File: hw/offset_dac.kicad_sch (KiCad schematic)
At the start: 35 parts, among them Q1 SSM6N35AFE, Q3 SSM6N35AFE, U22 TSV992A, U23 MCP47CVB02-E_UN

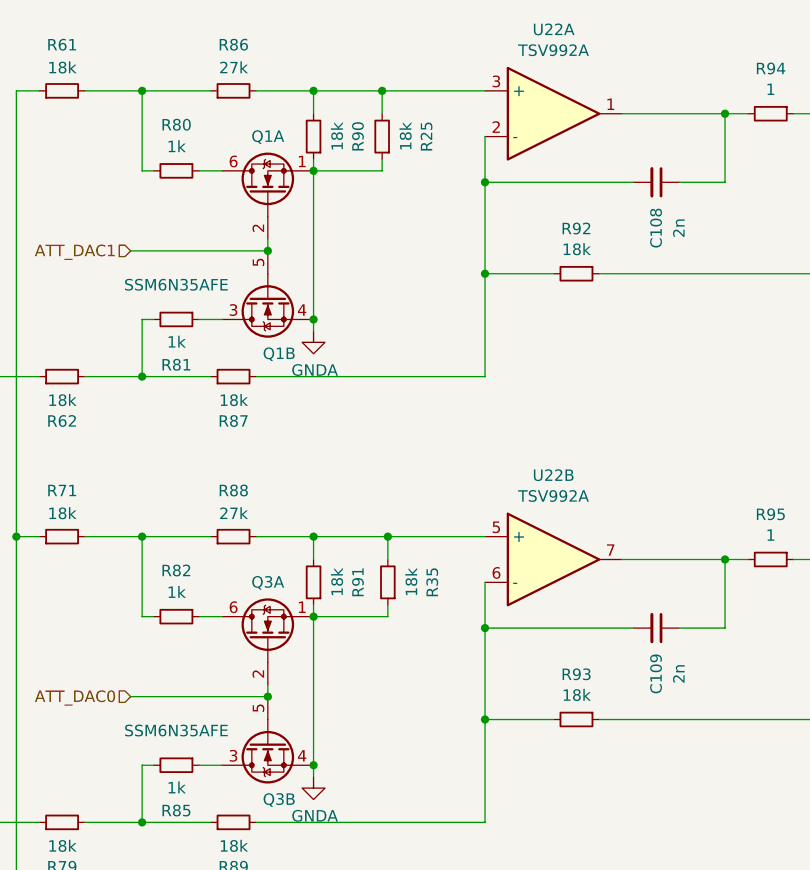
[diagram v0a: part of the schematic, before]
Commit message: Modified DAC resistors/range; connect + pull-up ADC SHDN
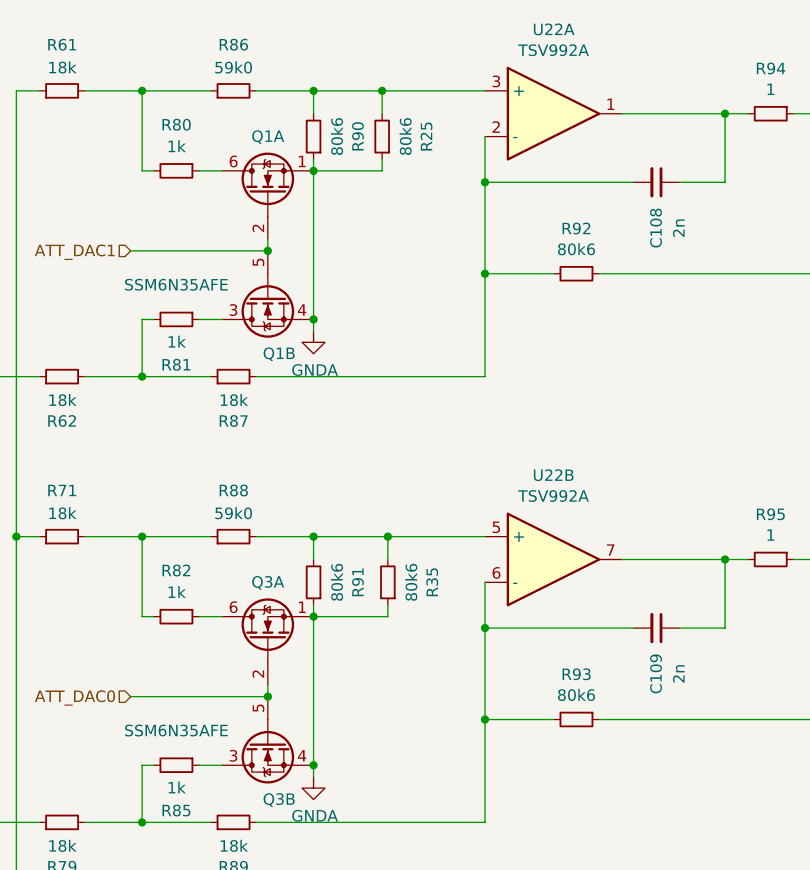
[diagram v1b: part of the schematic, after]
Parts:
- R25, R35, R90, R91, R92, R93: value 18k -> 80k6
- R86, R88: value 27k -> 59k0
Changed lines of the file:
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@@
       (effects (font (size 1.27 1.27)))
     )
-    (property "Value" "18k" (at 167.64 63.373 90)
+    (property "Value" "80k6" (at 167.64 63.373 90)
       (effects (font (size 1.27 1.27)))
     )
@@
       (effects (font (size 1.27 1.27)))
     )
-    (property "Value" "18k" (at 141.097 50.8 90)
+    (property "Value" "80k6" (at 141.097 50.8 90)
       (effects (font (size 1.27 1.27)))
     )
@@
       (effects (font (size 1.27 1.27)))
     )
-    (property "Value" "18k" (at 167.64 112.903 90)
+    (property "Value" "80k6" (at 167.64 112.903 90)
       (effects (font (size 1.27 1.27)))
     )
@@
       (effects (font (size 1.27 1.27)))
     )
-    (property "Value" "27k" (at 129.54 92.71 90)
+    (property "Value" "59k0" (at 129.54 92.71 90)
       (effects (font (size 1.27 1.27)))
     )
@@
       (effects (font (size 1.27 1.27)))
     )
-    (property "Value" "18k" (at 148.717 50.8 90)
+    (property "Value" "80k6" (at 148.717 50.8 90)
       (effects (font (size 1.27 1.27)))
     )
@@
       (effects (font (size 1.27 1.27)))
     )
-    (property "Value" "18k" (at 149.352 100.33 90)
+    (property "Value" "80k6" (at 149.352 100.33 90)
       (effects (font (size 1.27 1.27)))
     )
@@
       (effects (font (size 1.27 1.27)))
     )
-    (property "Value" "18k" (at 141.097 100.33 90)
+    (property "Value" "80k6" (at 141.097 100.33 90)
       (effects (font (size 1.27 1.27)))
     )
@@
       (effects (font (size 1.27 1.27)))
     )
-    (property "Value" "27k" (at 129.54 43.18 90)
-      (effects (font (size 1.27 1.27)))
-    )
+    (property "Value" "59k0" (at 129.54 43.18 90)
+      (effects (font (size 1.27 1.27)))
+    )

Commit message: renaming, comments, part/vendor and other cosmetics (no pcb change)
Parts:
- U22: Manufacturer (none) -> ST; Part (none) -> TSV992IQ2
- U23: Part MCP47CVB02-E_UN -> MCP47CVB02-E/UN
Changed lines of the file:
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@@
       (effects (font (size 1.27 1.27)) hide)
     )
-    (property "Part" "MCP47CVB02-E_UN" (at 105.41 152.4 0)
+    (property "Part" "MCP47CVB02-E/UN" (at 105.41 152.4 0)
       (effects (font (size 1.27 1.27)) hide)
     )
@@
       (effects (font (size 1.27 1.27)) hide)
     )
+    (property "Part" "TSV992IQ2" (at 165.1 48.26 0)
+      (effects (font (size 1.27 1.27)) hide)
+    )
+    (property "Manufacturer" "ST" (at 165.1 48.26 0)
+      (effects (font (size 1.27 1.27)) hide)
+    )
     (pin "1")
     (pin "2")
@@
     )
     (property "Sim.Pins" "1=out1 2=in1- 3=in1+ 4=vee 5=in2+ 6=in2- 7=out2 8=vcc" (at 165.1 97.79 0)
+      (effects (font (size 1.27 1.27)) hide)
+    )
+    (property "Part" "TSV992IQ2" (at 165.1 97.79 0)
+      (effects (font (size 1.27 1.27)) hide)
+    )
+    (property "Manufacturer" "ST" (at 165.1 97.79 0)
       (effects (font (size 1.27 1.27)) hide)
     )
@@
       (effects (font (size 1.27 1.27)) hide)
     )
+    (property "Part" "TSV992IQ2" (at 55.88 58.42 0)
+      (effects (font (size 1.27 1.27)) hide)
+    )
+    (property "Manufacturer" "ST" (at 55.88 58.42 0)
+      (effects (font (size 1.27 1.27)) hide)
+    )

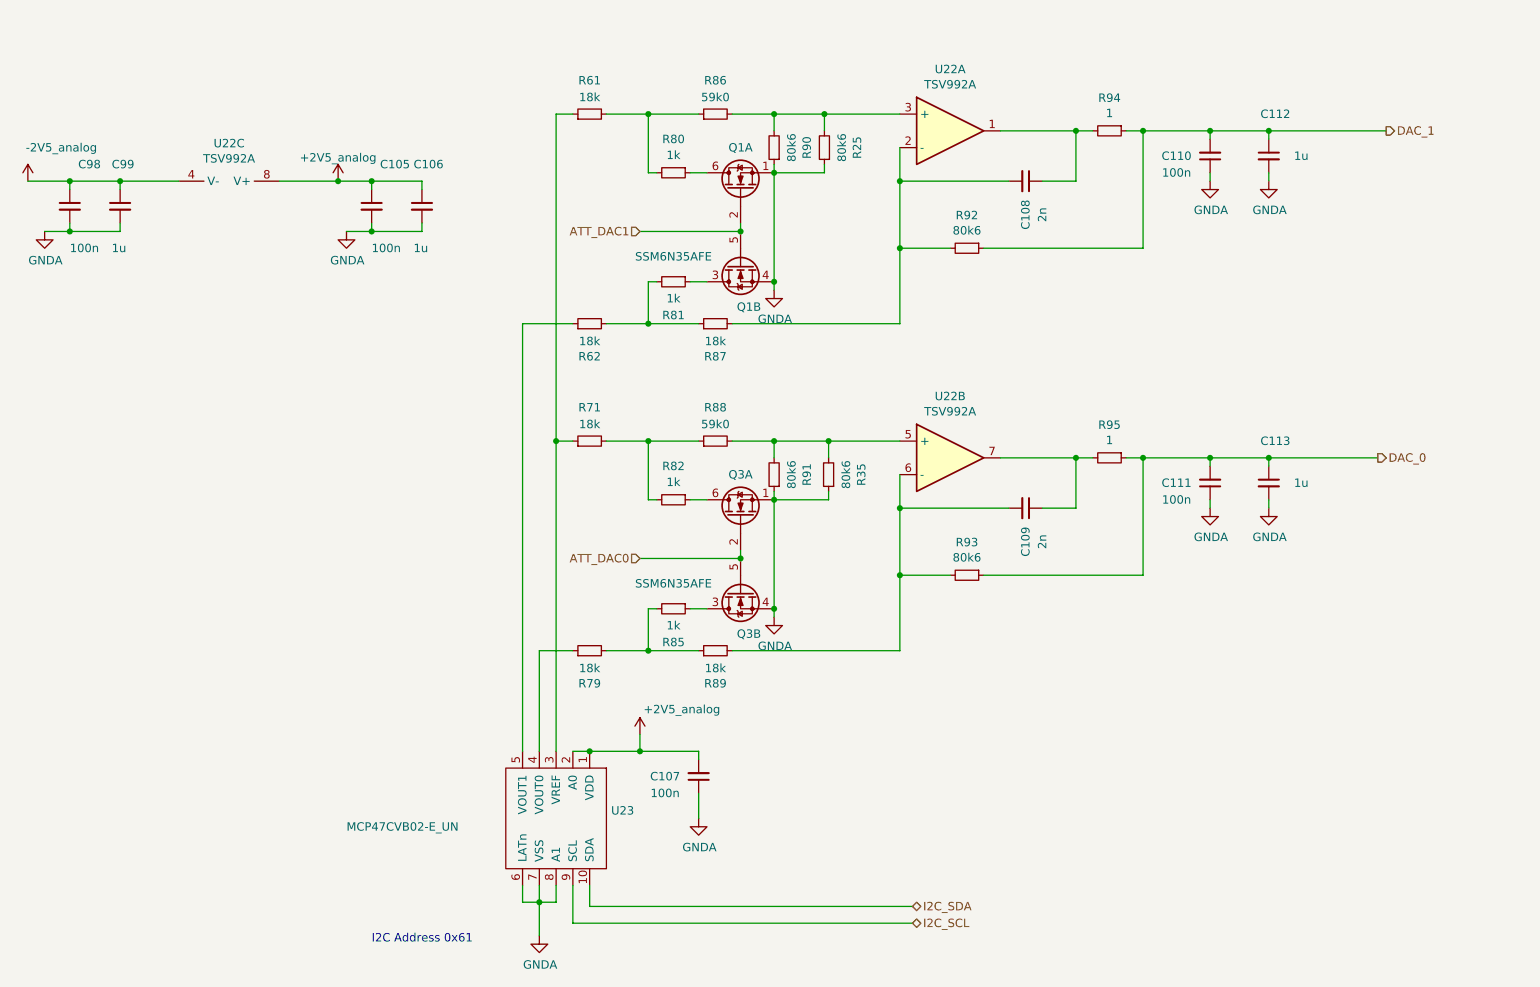
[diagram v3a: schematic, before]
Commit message: DAC noise improvements
 - increased C108, C109 from 2n to 100n
 - added C147, C148 (100n) parallel to R25, R35, respectively.
   Recycled pads of second 80k6 resistors for new capacitors
   so that the layout + stencil stay the same.

Significantly improves noise on 10kHz-100kHz band.
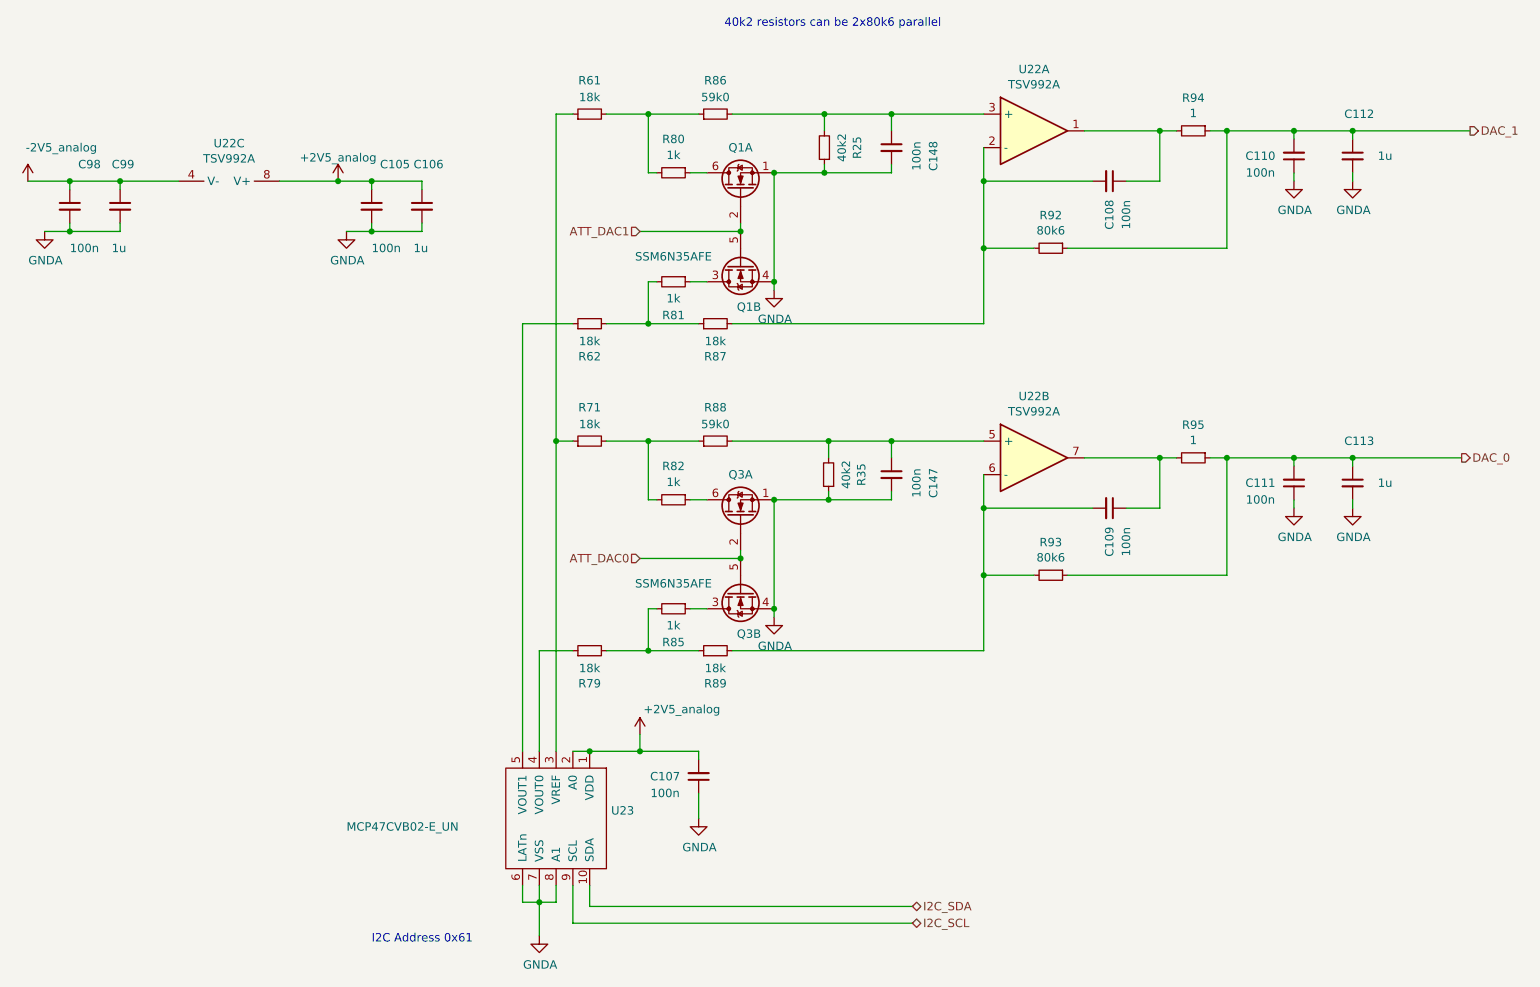
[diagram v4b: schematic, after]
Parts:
- removed R90, R91: 80k6, Resistor_SMD:R_0603_1608Metric, symbol Device:R_Small
- added C147, C148: 100n, Capacitor_SMD:C_0603_1608Metric, symbol Device:C_Small
- C108, C109: value 2n -> 100n; Manufacturer (none) -> Samsung; Part (none) -> CL10B104KB8NFN
- R25, R35: value 80k6 -> 40k2
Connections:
- net GNDA: now also C147.2, C148.2
- net at R25.2, R86.2, U22.3 (+): now also C148.1
- net at R35.2, R88.2, U22.5 (+): now also C147.1
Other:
- note added: "40k2 resistors can be 2x80k6 parallel"
- moved on the sheet: C108, C109, C110, C111, C112, C113, R92, R93, R94, R95, U22A, U22B

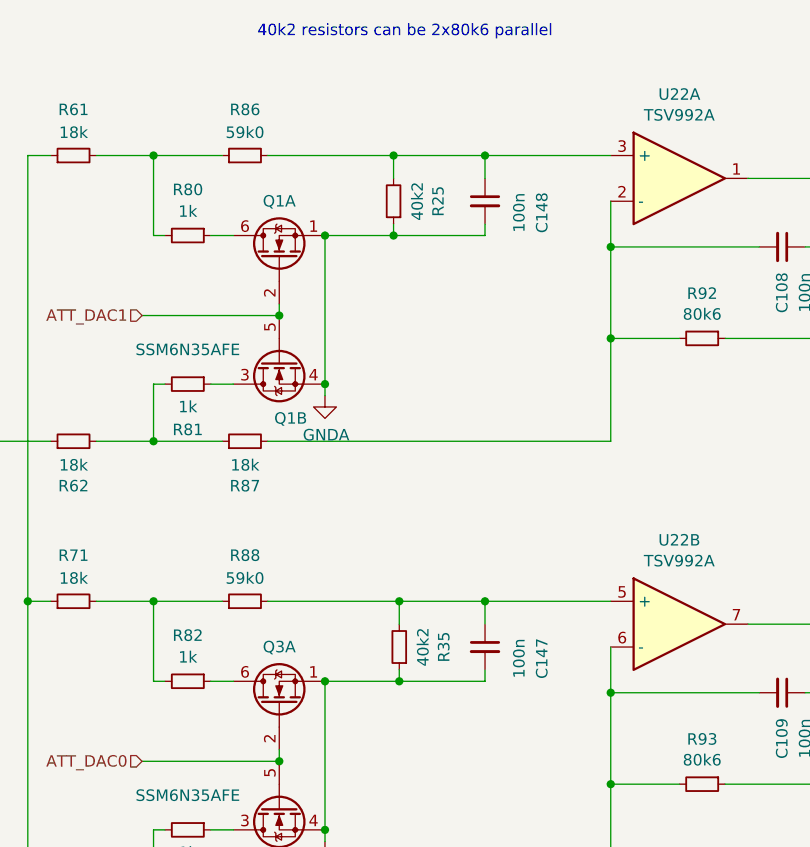
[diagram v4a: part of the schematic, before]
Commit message: prep-work to move front-end into separate project (for replication)
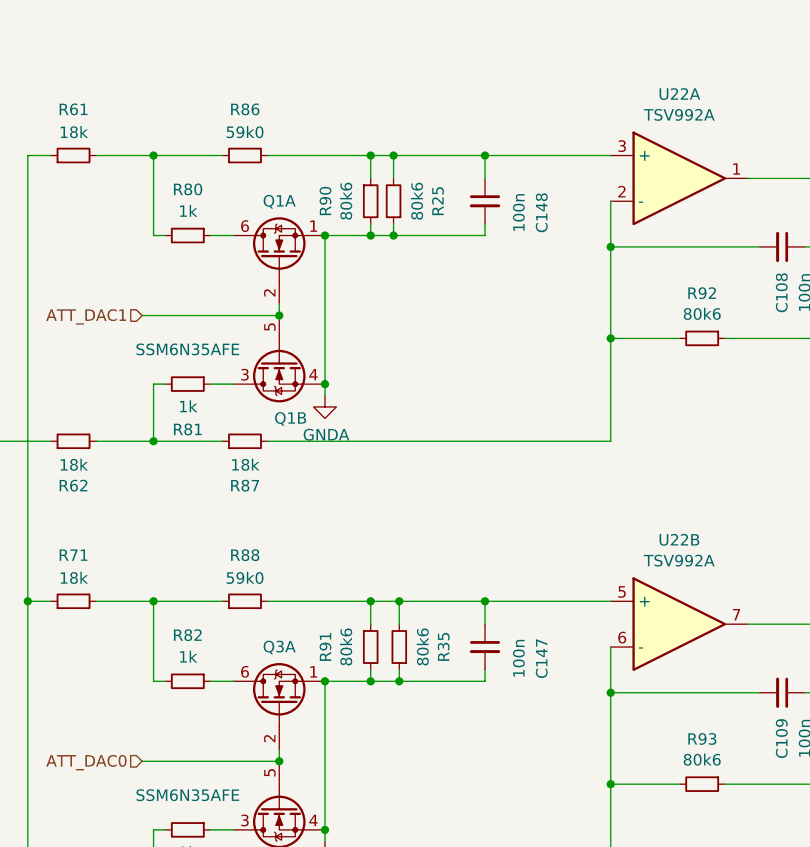
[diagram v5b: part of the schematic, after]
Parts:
- added R90, R91: 80k6, Resistor_SMD:R_0603_1608Metric, symbol Device:R_Small
- R25, R35: value 40k2 -> 80k6
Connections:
- net GNDA: now also R90.2, R91.2
- net at C148.1, R25.2, R86.2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: now also R90.1
- net at C147.1, R35.2, R88.2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: now also R91.1
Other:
- note removed: "40k2 resistors can be 2x80k6 parallel"
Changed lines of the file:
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@@
 	)
 	(junction
+		(at 143.51 54.61)
+		(diameter 0)
+		(color 0 0 0 0)
+	)
+	(junction
+		(at 143.51 104.14)
+		(diameter 0)
+		(color 0 0 0 0)
+	)
+	(junction
+		(at 143.51 45.72)
+		(diameter 0)
+		(color 0 0 0 0)
+	)
+	(junction
 		(at 138.43 54.61)
 		(diameter 0)
@@
 	)
 	(junction
+		(at 143.51 95.25)
+		(diameter 0)
+		(color 0 0 0 0)
+	)
+	(junction
 		(at 102.87 165.1)
 		(diameter 0)
@@
 	(wire
 		(pts
+			(xy 143.51 54.61) (xy 138.43 54.61)
+		)
+		(stroke
+			(width 0)
+			(type default)
+		)
+	)
+	(wire
+		(pts
 			(xy 226.06 54.61) (xy 226.06 55.88)
 		)
@@
 	(wire
 		(pts
+			(xy 143.51 45.72) (xy 146.05 45.72)
+		)
+		(stroke
+			(width 0)
+			(type default)
+		)
+	)
+	(wire
+		(pts
 			(xy 125.73 104.14) (xy 128.27 104.14)
 		)
@@
 	(wire
 		(pts
-			(xy 132.08 45.72) (xy 146.05 45.72)
+			(xy 132.08 45.72) (xy 143.51 45.72)
 		)
 		(stroke
@@
 	(wire
 		(pts
+			(xy 143.51 45.72) (xy 143.51 48.26)
+		)
+		(stroke
+			(width 0)
+			(type default)
+		)
+	)
+	(wire
+		(pts
 			(xy 156.21 102.87) (xy 156.21 104.14)
 		)
@@
 	(wire
 		(pts
+			(xy 143.51 104.14) (xy 146.685 104.14)
+		)
+		(stroke
+			(width 0)
+			(type default)
+		)
+	)
+	(wire
+		(pts
 			(xy 31.75 62.23) (xy 31.75 63.5)
 		)
@@
 	(wire
 		(pts
-			(xy 138.43 104.14) (xy 146.685 104.14)
+			(xy 138.43 104.14) (xy 143.51 104.14)
 		)
 		(stroke
@@
 	(wire
 		(pts
-			(xy 146.05 54.61) (xy 138.43 54.61)
+			(xy 146.05 54.61) (xy 143.51 54.61)
 		)
 		(stroke
@@
 	(wire
 		(pts
-			(xy 132.08 95.25) (xy 146.685 95.25)
+			(xy 132.08 95.25) (xy 143.51 95.25)
+		)
+		(stroke
+			(width 0)
+			(type default)
+		)
+	)
+	(wire
+		(pts
+			(xy 143.51 95.25) (xy 146.685 95.25)
 		)
 		(stroke
@@
 	(wire
 		(pts
+			(xy 143.51 95.25) (xy 143.51 97.79)
+		)
+		(stroke
+			(width 0)
+			(type default)
+		)
+	)
+	(wire
+		(pts
 			(xy 85.09 62.23) (xy 85.09 63.5)
 		)
@@
 	(wire
 		(pts
+			(xy 143.51 102.87) (xy 143.51 104.14)
+		)
+		(stroke
+			(width 0)
+			(type default)
+		)
+	)
+	(wire
+		(pts
 			(xy 119.38 120.65) (xy 120.65 120.65)
 		)
@@
 	(wire
 		(pts
+			(xy 143.51 53.34) (xy 143.51 54.61)
+		)
+		(stroke
+			(width 0)
+			(type default)
+		)
+	)
+	(wire
+		(pts
 			(xy 133.35 62.23) (xy 133.35 63.5)
 		)
@@
 		)
 	)
-	(text "40k2 resistors can be 2x80k6 parallel"
-		(exclude_from_sim no)
-		(at 147.32 32.004 0)
-		(effects
-			(font
-				(size 1.27 1.27)
-			)
-		)
-	)
 	(text "I2C Address 0x61"
 		(exclude_from_sim no)
@@
 	(symbol
 		(lib_id "Device:R_Small")
+		(at 143.51 100.33 0)
+		(unit 1)
+		(exclude_from_sim no)
+		(in_bom yes)
+		(on_board yes)
+		(dnp no)
+		(property "Reference" "R91"
+			(at 138.5316 100.33 90)
+			(effects
+				(font
+					(size 1.27 1.27)
+				)
+			)
+		)
+		(property "Value" "80k6"
+			(at 140.843 100.33 90)
+			(effects
+				(font
+					(size 1.27 1.27)
+				)
+			)
+		)
+		(property "Footprint" "Resistor_SMD:R_0603_1608Metric"
+			(at 143.51 100.33 0)
+			(effects
+				(font
+					(size 1.27 1.27)
+				)
+				(hide yes)
+			)
+		)
+		(property "Datasheet" "~"
+			(at 143.51 100.33 0)
+			(effects
+				(font
+					(size 1.27 1.27)
+				)
+				(hide yes)
+			)
+		)
+		(property "Description" ""
+			(at 143.51 100.33 0)
+			(effects
+				(font
+					(size 1.27 1.27)
+				)
+				(hide yes)
+			)
+		)
+		(pin "1"
+		)
+		(pin "2"
+		)
+		(instances
+			(project "usbadc"
+				(path "/7c8a1f8d-8834-4c9b-aaae-1f231e9b09a1/c969de1a-32a7-4770-b1aa-e527a627ef90/413eeb87-85d0-4a61-9245-920a92a97234"
+					(reference "R91")
+					(unit 1)
+				)
+			)
+		)
+	)
+	(symbol
+		(lib_id "Device:R_Small")
 		(at 129.54 95.25 90)
 		(unit 1)
@@
 			)
 		)
-		(property "Value" "40k2"
+		(property "Value" "80k6"
 			(at 148.717 50.8 90)
 			(effects
@@
 			)
 		)
-		(property "Value" "40k2"
+		(property "Value" "80k6"
 			(at 149.352 100.33 90)
 			(effects
@@
 					(unit 1)
 				)
+			)
+		)
+	)
+	(symbol
+		(lib_id "Device:R_Small")
+		(at 143.51 50.8 0)
+		(unit 1)
+		(exclude_from_sim no)
+		(in_bom yes)
+		(on_board yes)
+		(dnp no)
+		(property "Reference" "R90"
+			(at 138.5316 50.8 90)
+			(effects
+				(font
+					(size 1.27 1.27)
+				)
+			)
+		)
+		(property "Value" "80k6"
+			(at 140.843 50.8 90)
+			(effects
+				(font
+					(size 1.27 1.27)
+				)
+			)
+		)
+		(property "Footprint" "Resistor_SMD:R_0603_1608Metric"
+			(at 143.51 50.8 0)
+			(effects
+				(font
+					(size 1.27 1.27)
+				)
+				(hide yes)
+			)
+		)
+		(property "Datasheet" "~"
+			(at 143.51 50.8 0)
+			(effects
+				(font
+					(size 1.27 1.27)
+				)
+				(hide yes)
+			)
+		)
+		(property "Description" ""
+			(at 143.51 50.8 0)
+			(effects
+				(font
+					(size 1.27 1.27)
+				)
+				(hide yes)
+			)
+		)
+		(pin "1"
+		)
+		(pin "2"
+		)
+		(instances
+			(project "usbadc"
+				(path "/7c8a1f8d-8834-4c9b-aaae-1f231e9b09a1/c969de1a-32a7-4770-b1aa-e527a627ef90/413eeb87-85d0-4a61-9245-920a92a97234"
+					(reference "R90")
+					(unit 1)
+				)
